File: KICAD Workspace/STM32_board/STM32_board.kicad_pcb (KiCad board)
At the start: 2 copper layers, 171.4 x 151.8 mm, 28 parts, among them J1 Power connector, J2 High side connector, J3 Sensors connector, J4 LCD interface, J5 Low side connector, J6 3v3_out, J7 Joystick connector, J8 External Pins, J9 UART module, U1 CD4050BE, U2 LM7805_TO220, U3 LP2950-3.3_TO92

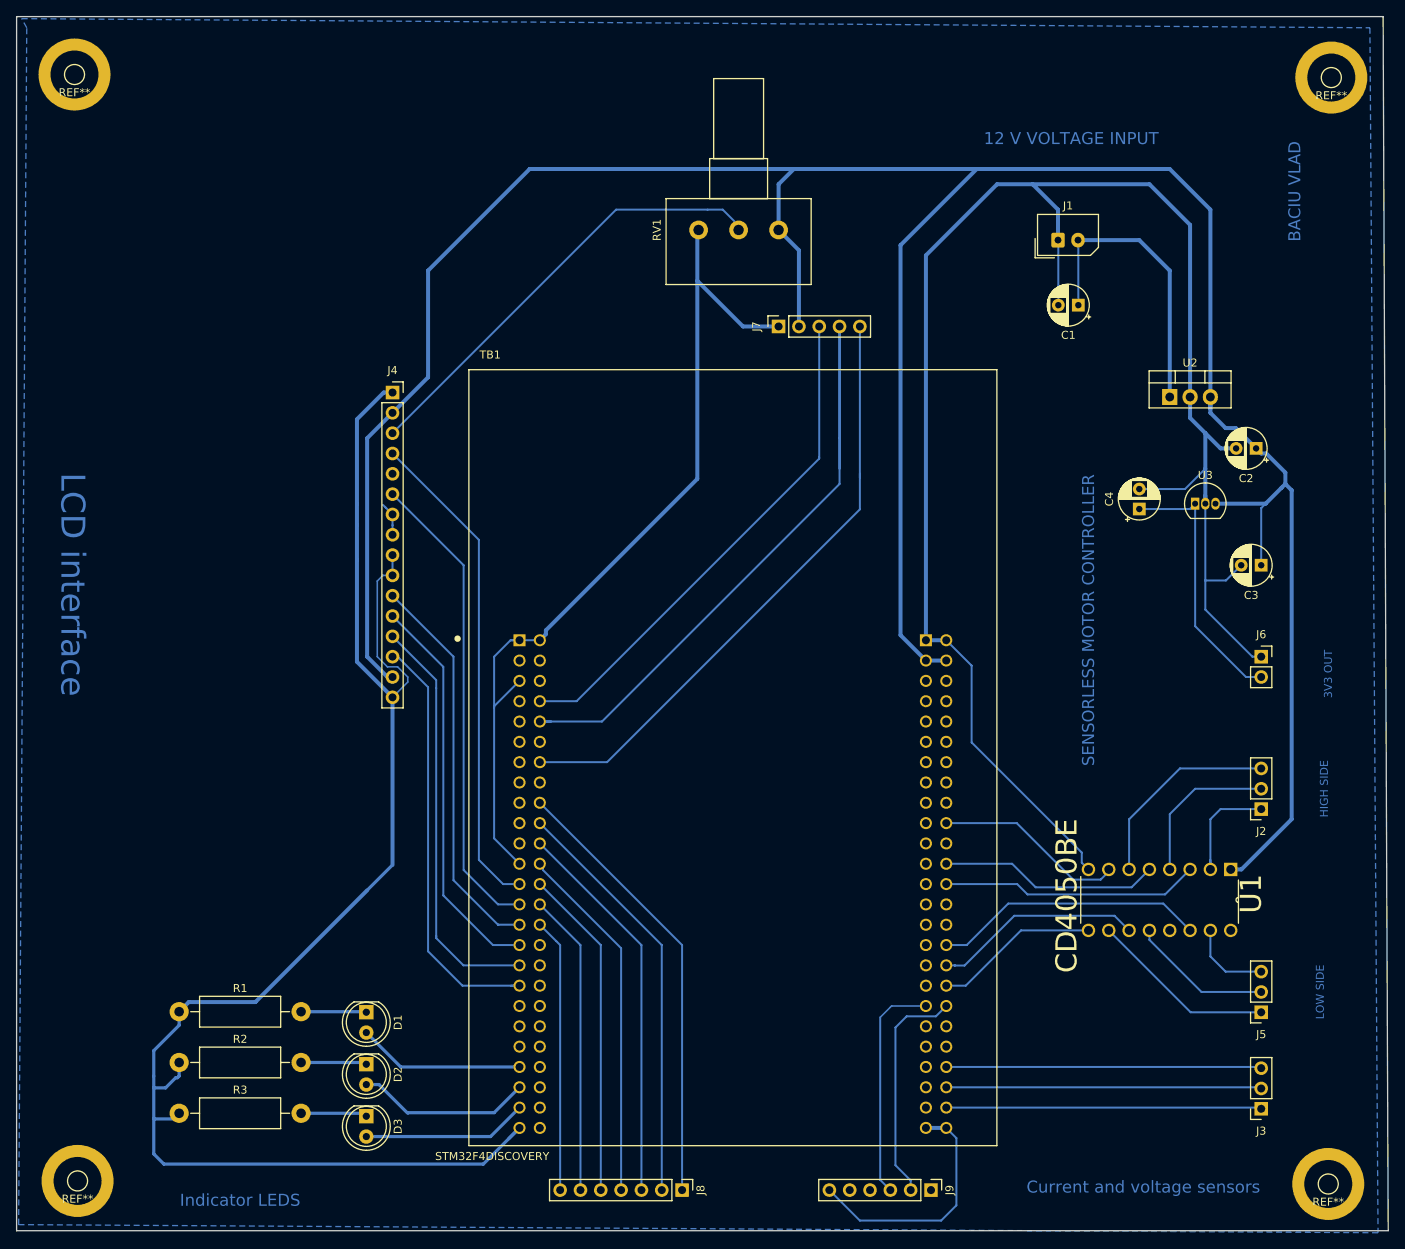
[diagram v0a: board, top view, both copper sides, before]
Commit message: Modifications of layout. Added some connectors, deleted others, pins connections changed
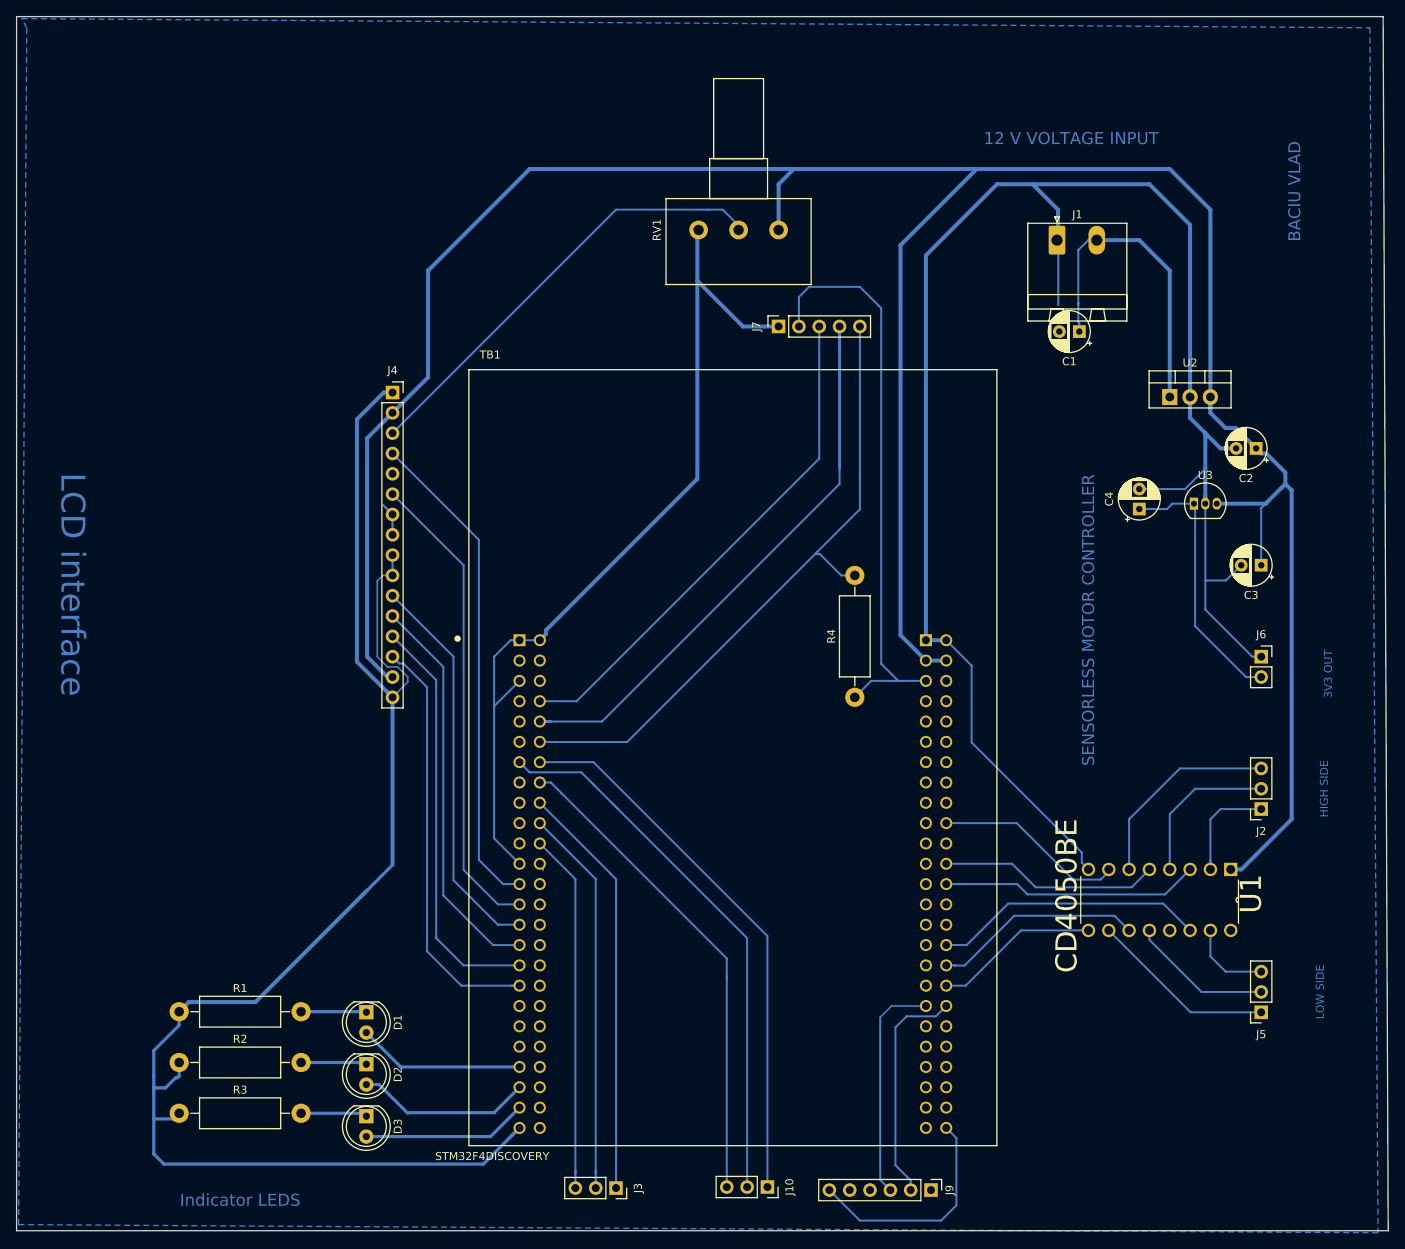
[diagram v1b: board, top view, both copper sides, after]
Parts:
- removed J8: External Pins, Connector_PinHeader_2.54mm:PinHeader_1x07_P2.54mm_Vertical
- removed REF** (x4): Pin_D1.0mm_L10.0mm, Connector_Pin:Pin_D1.0mm_L10.0mm
- added J10: Low side connector, Connector_PinSocket_2.54mm:PinSocket_1x03_P2.54mm_Vertical, F.Cu at (111.3, 160.3)
- added R4: R, Resistor_THT:R_Axial_DIN0411_L9.9mm_D3.6mm_P15.24mm_Horizontal, F.Cu at (122.2, 99.1)
- J1: footprint Connector_Molex:Molex_SPOX_5267-02A_1x02_P2.50mm_Vertical -> Connector_Phoenix_MSTB:PhoenixContact_MSTBA_2,5_2-G-5,08_1x02_P5.08mm_Horizontal
- moved J3 81.3 mm to (92.3, 160.4), turned to 270 degrees
- moved C1 3.30 mm to (150.2, 53.3)
- moved J1 0.13 mm to (147.4, 41.9)
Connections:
- J7 pad 2: /5V -> /3V
- TB1 pad P1_12: Net-(TB1-PadP1_12) -> /JoystickButton
- TB1 pad P1_13: Net-(TB1-PadP1_13) -> /EXT_1
- TB1 pad P1_14: /JoystickButton -> /EXT_0
- TB1 pad P1_16: Net-(TB1-PadP1_16) -> /EXT_2
- TB1 pad P1_18: /EXT_1 -> /ADC_BATTERY
- TB1 pad P1_20: /EXT_2 -> /CURRENT_SENSOR
- TB1 pad P1_22: /EXT_3 -> /READ_BATTERY
- TB1 pad P2_44: /READ_BATTERY -> Net-(TB1-PadP2_44)
- TB1 pad P2_46: /CURRENT_SENSOR -> Net-(TB1-PadP2_46)
- TB1 pad P2_48: /ADC_BATTERY -> Net-(TB1-PadP2_48)
- TB1 pad P2_5: Net-(TB1-PadP2_5) -> /3V
- TB1 pad P2_6: Net-(TB1-PadP2_5) -> /3V
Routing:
- net /3V: track 0.00 -> 72.7 mm
- net /EXT_0: track 0.00 -> 69.9 mm
- net /EXT_3: track 48.6 -> 0.00 mm
- net /EXT_4: track 45.4 -> 1.34 mm
- net /EXT_5: track 41.4 -> 0.00 mm
- net /EXT_6: track 37.8 -> 0.00 mm
- net /EXT_7: track 34.2 -> 0.00 mm
- net /EXT_1: track 55.8 -> 70.9 mm
- net /ADC_BATTERY: track 39.4 -> 53.4 mm
- net /5V: track 366.5 -> 353.4 mm
- net /EXT_2: track 52.2 -> 62.1 mm
- net /CURRENT_SENSOR: track 39.4 -> 49.1 mm
- net /READ_BATTERY: track 39.4 -> 45.3 mm
- net /JoystickButton: track 76.4 -> 81.8 mm
- net /12V: track 37.0 -> 39.8 mm
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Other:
- board text removed: "Current and voltage sensors"

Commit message: Added some modifications to UART connector.
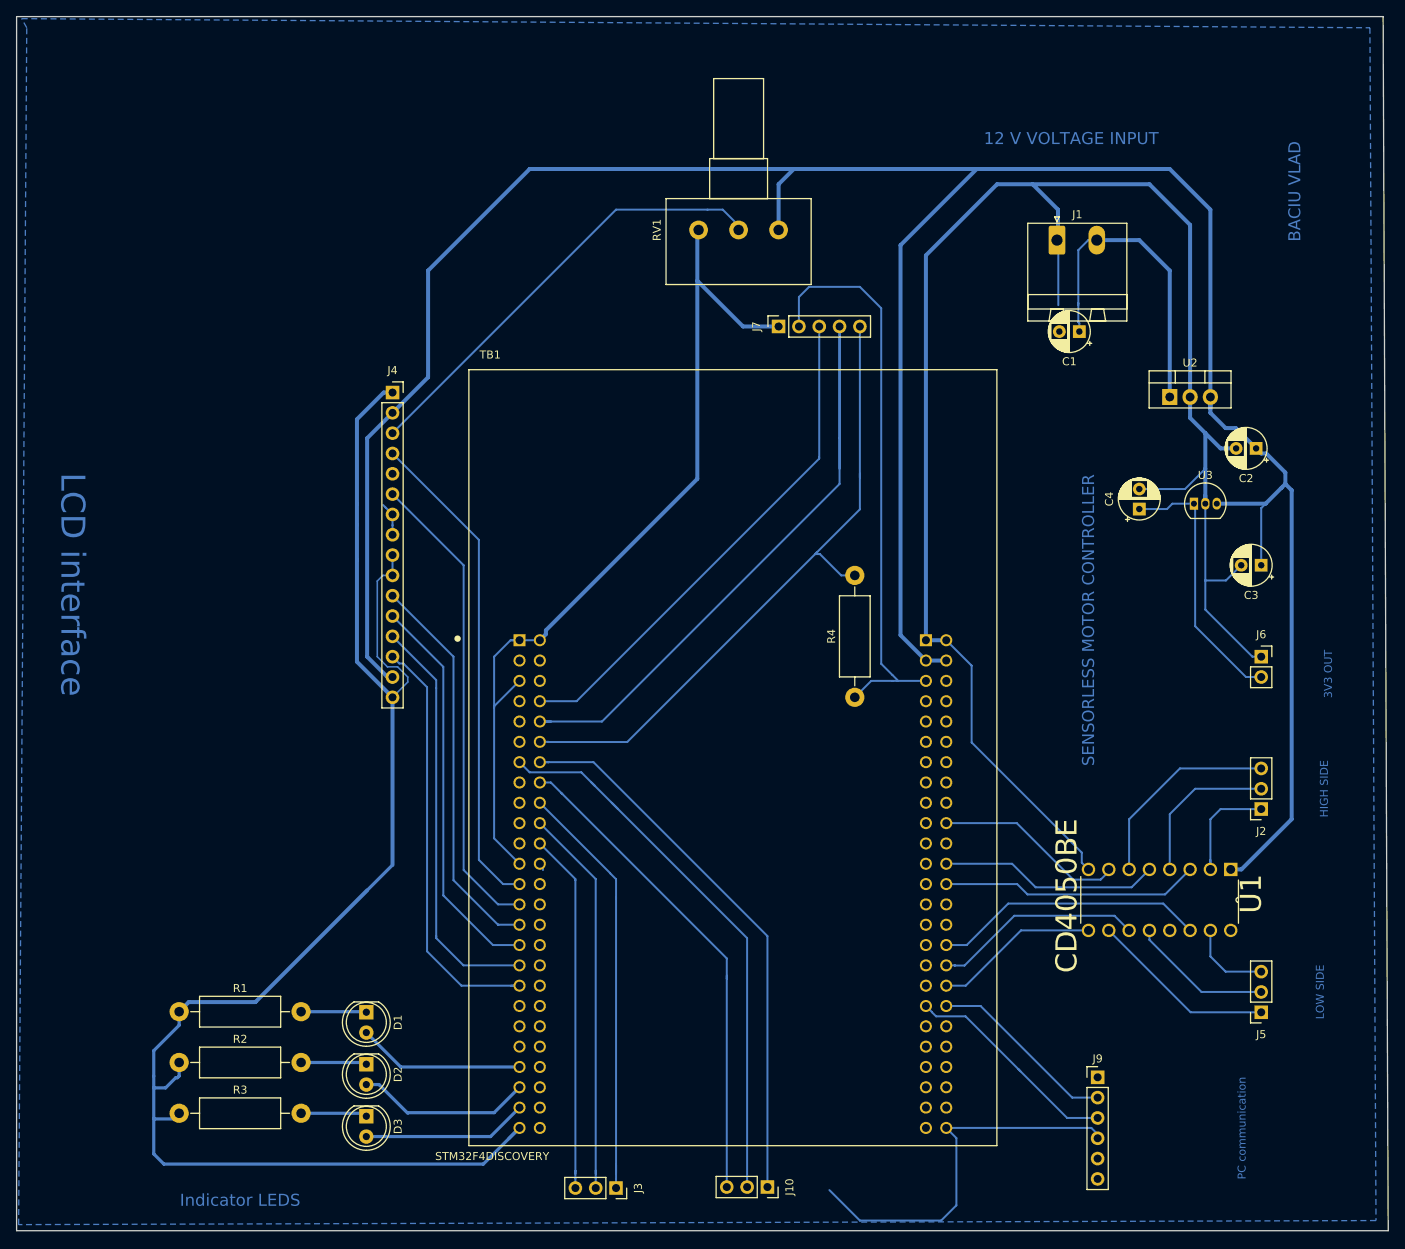
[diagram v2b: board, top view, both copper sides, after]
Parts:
- moved J9 25.2 mm to (152.5, 146.6), turned to 0 degrees
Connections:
- J3 pad 1: /ADC_BATTERY -> /CURRENT_SENSOR
- J3 pad 2: /CURRENT_SENSOR -> /ADC_BATTERY
- TB1 pad P1_18: /ADC_BATTERY -> /CURRENT_SENSOR
- TB1 pad P1_20: /CURRENT_SENSOR -> /ADC_BATTERY
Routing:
- net /GND: track 603.7 -> 622.6 mm
- net /UART2_RX: track 28.6 -> 23.7 mm
- net /CURRENT_SENSOR: track 49.1 -> 53.4 mm
- net /ADC_BATTERY: track 53.4 -> 49.1 mm
- net /UART1_TX: track 28.4 -> 27.6 mm
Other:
- board text added: "PC communication"

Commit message: Final version for printing (i hope)
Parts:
- added J11: Output pins, Connector_PinSocket_2.54mm:PinSocket_1x03_P2.54mm_Vertical, F.Cu at (126.0, 160.4)
- added J8: Output pins, Connector_PinSocket_2.54mm:PinSocket_1x03_P2.54mm_Vertical, F.Cu at (89.8, 160.1)
- C1, C2, C3, C4: footprint Capacitor_THT:CP_Radial_D5.0mm_P2.50mm -> Capacitor_THT:CP_Radial_D8.0mm_P3.50mm
- moved J3 7.49 mm to (99.8, 160.3)
- moved J1 5.08 mm to (152.5, 42.0), turned to 180 degrees
- moved J6 2.55 mm to (173.2, 96.5)
- moved C4 1.53 mm to (156.2, 75.7)
- moved U3 0.15 mm to (164.9, 74.9)
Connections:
- J1 pad 1: /GND -> /12V
- J1 pad 2: /12V -> /GND
- J6 pad 1: /GND -> /3V3
- J6 pad 2: /3V3 -> /GND
- TB1 pad P1_24: /EXT_4 -> Net-(TB1-PadP1_24)
- TB1 pad P2_45: Net-(TB1-PadP2_45) -> /EXT_3
- TB1 pad P2_47: Net-(TB1-PadP2_47) -> /EXT_4
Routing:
- net /EXT_5: track 0.00 -> 41.4 mm
- net /EXT_6: track 0.00 -> 37.0 mm
- net /EXT_7: track 0.00 -> 33.4 mm
- net /EXT_3: track 0.00 -> 17.1 mm
- net /EXT_4: track 1.34 -> 13.5 mm
- net /READ_BATTERY: track 45.3 -> 48.6 mm
- net /ADC_BATTERY: track 49.1 -> 52.2 mm
- net /3V3: track 33.3 -> 35.7 mm
- net /CURRENT_SENSOR: track 53.4 -> 55.1 mm
- net /5V: track 353.4 -> 351.9 mm
- net /GND: track 622.6 -> 624.0 mm
- net Net-(TB1-PadP1_24): track 0.00 -> 0.94 mm
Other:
- board size 171.4 x 151.8 mm -> 171.4 x 138.7 mm
- board text added: "12V IN"
- board text removed: "12 V VOLTAGE INPUT"
